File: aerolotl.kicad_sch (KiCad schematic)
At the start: 0 parts

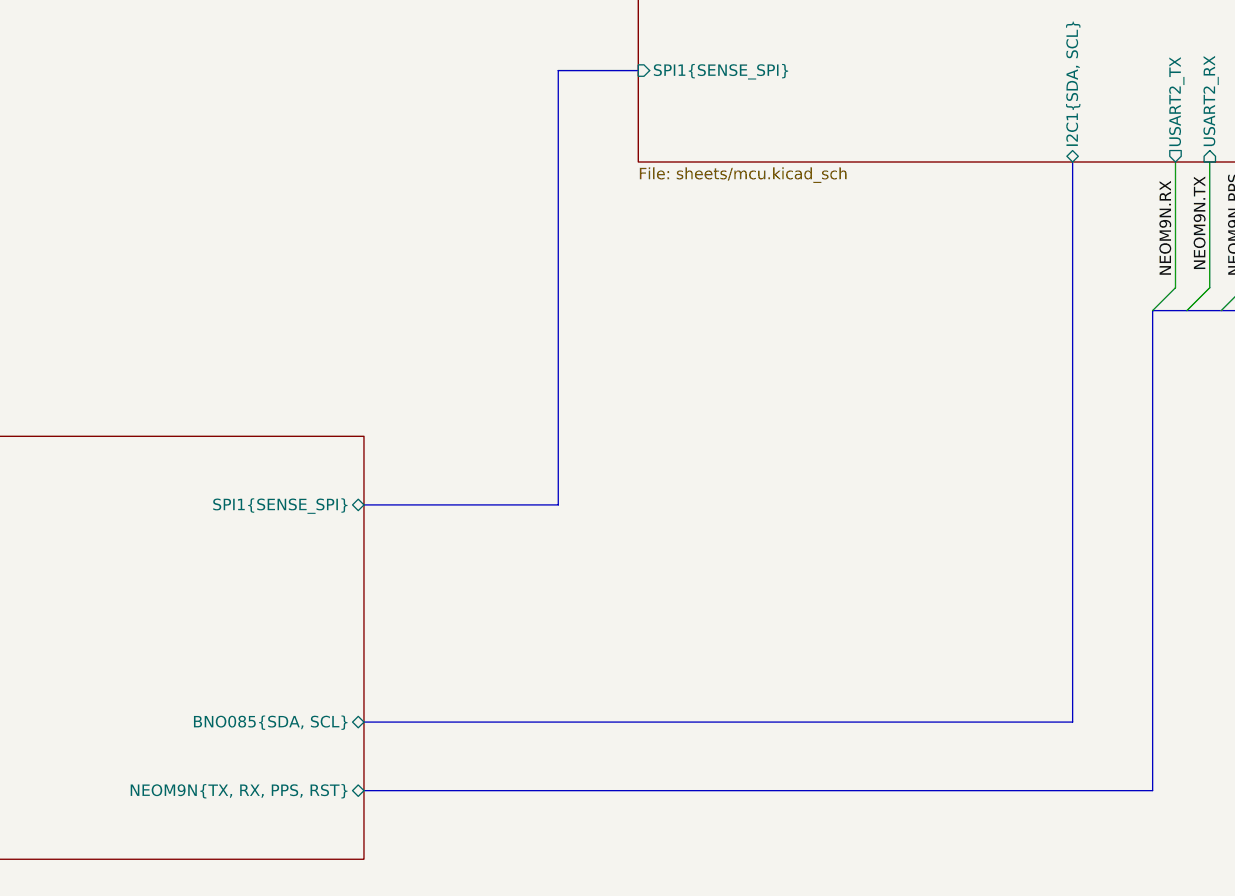
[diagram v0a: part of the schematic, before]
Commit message: solved reverse polarity w pmos and tvs clamp
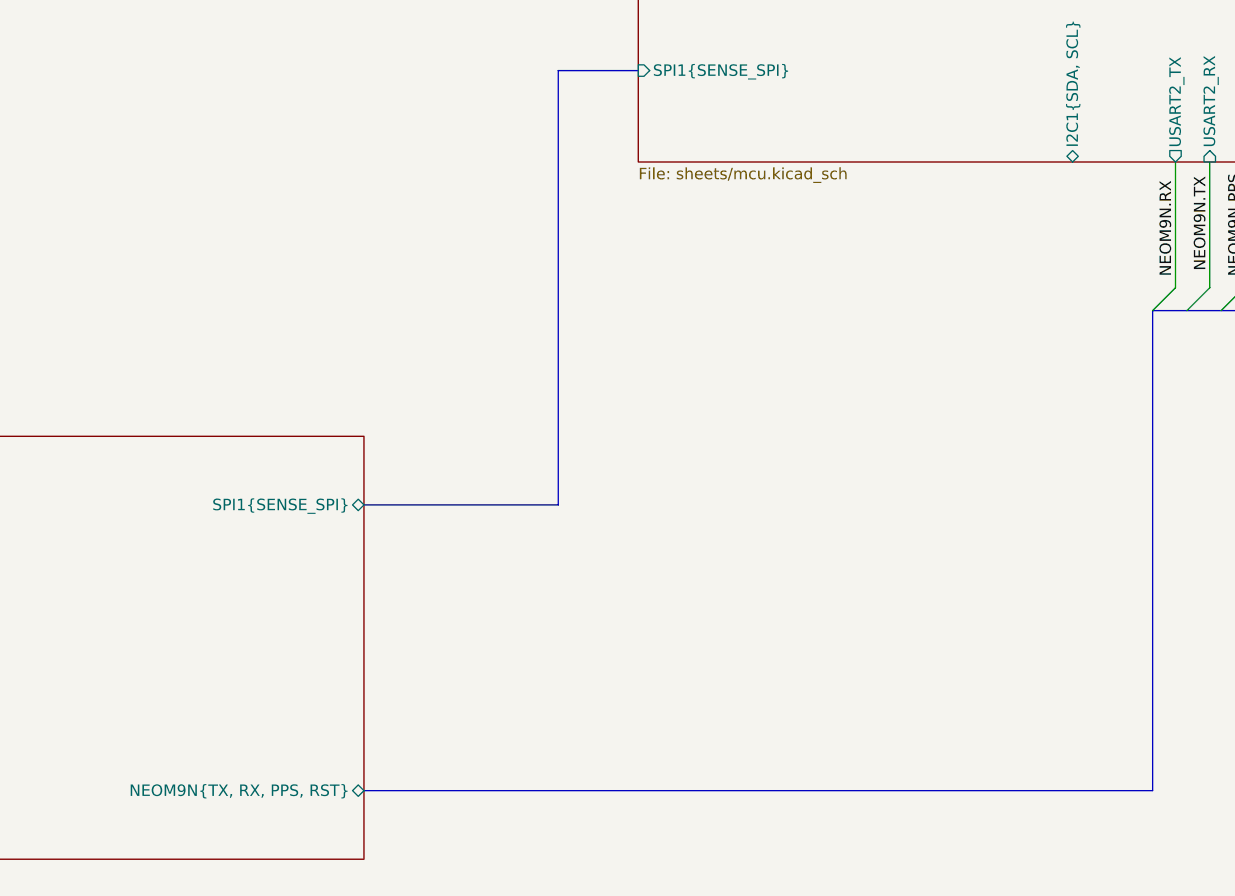
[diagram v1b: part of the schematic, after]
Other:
- sheet Sensors ports: added none; removed BNO085{SDA, SCL}
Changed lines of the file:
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@@
 	(bus_alias "SENSE_SPI"
 		(members "SCK" "MISO" "MOSI" "CS_345" "CS_375" "CS_BMP" "INT_345" "INT_375"
-			"INT_BMP"
+			"INT_BMP" "CS_IMU_ACC" "CS_IMU_GYRO" "INT_IMU_ACC" "INT_IMU_GYRO"
 		)
 	)
@@
 	(bus
 		(pts
-			(xy 182.88 240.03) (xy 104.14 240.03)
-		)
-		(stroke
-			(width 0)
-			(type default)
-		)
-	)
-	(bus
-		(pts
 			(xy 250.19 97.79) (xy 293.37 97.79)
 		)
@@
 		(pts
 			(xy 125.73 167.64) (xy 134.62 167.64)
-		)
-		(stroke
-			(width 0)
-			(type default)
-		)
-	)
-	(bus
-		(pts
-			(xy 182.88 177.8) (xy 182.88 240.03)
 		)
 		(stroke
@@
 			)
 		)
-		(pin "BNO085{SDA, SCL}" bidirectional
-			(at 104.14 240.03 0)
-			(effects
-				(font
-					(size 1.27 1.27)
-				)
-				(justify right)
-			)
-		)
